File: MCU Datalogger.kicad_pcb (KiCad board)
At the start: 2 copper layers, 52.8 x 34.3 mm, 30 parts, among them J1 Conn_01x04_Pin, J2 Conn_01x09_Pin, J3 Conn_01x04_Pin, J4 Conn_02x03_Odd_Even, U1 24LC1025, U2 DS1337S_, U3 24LC1025, U4 ATMEGA328P-AU, Y1 32.768 KHz, Y2 16 MHz

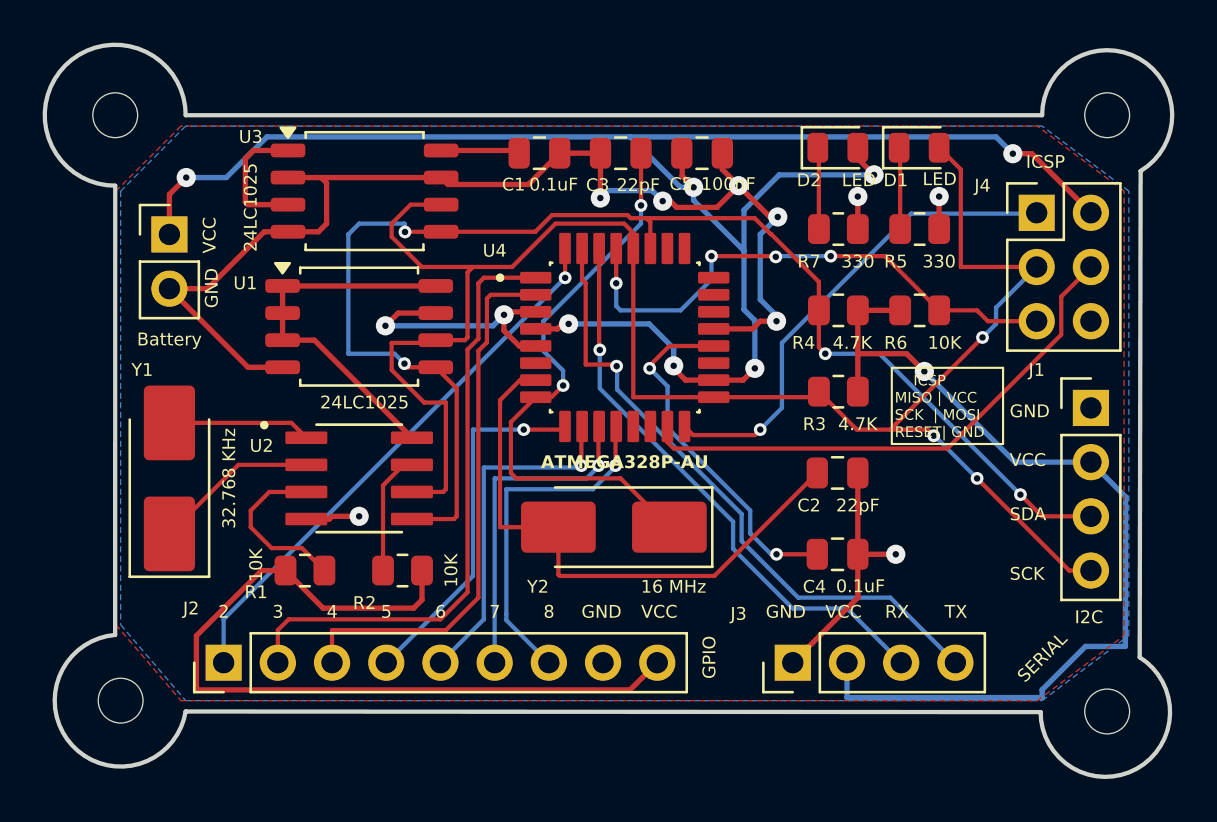
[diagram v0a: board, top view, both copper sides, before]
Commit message: Completed 4-layer PCB routing
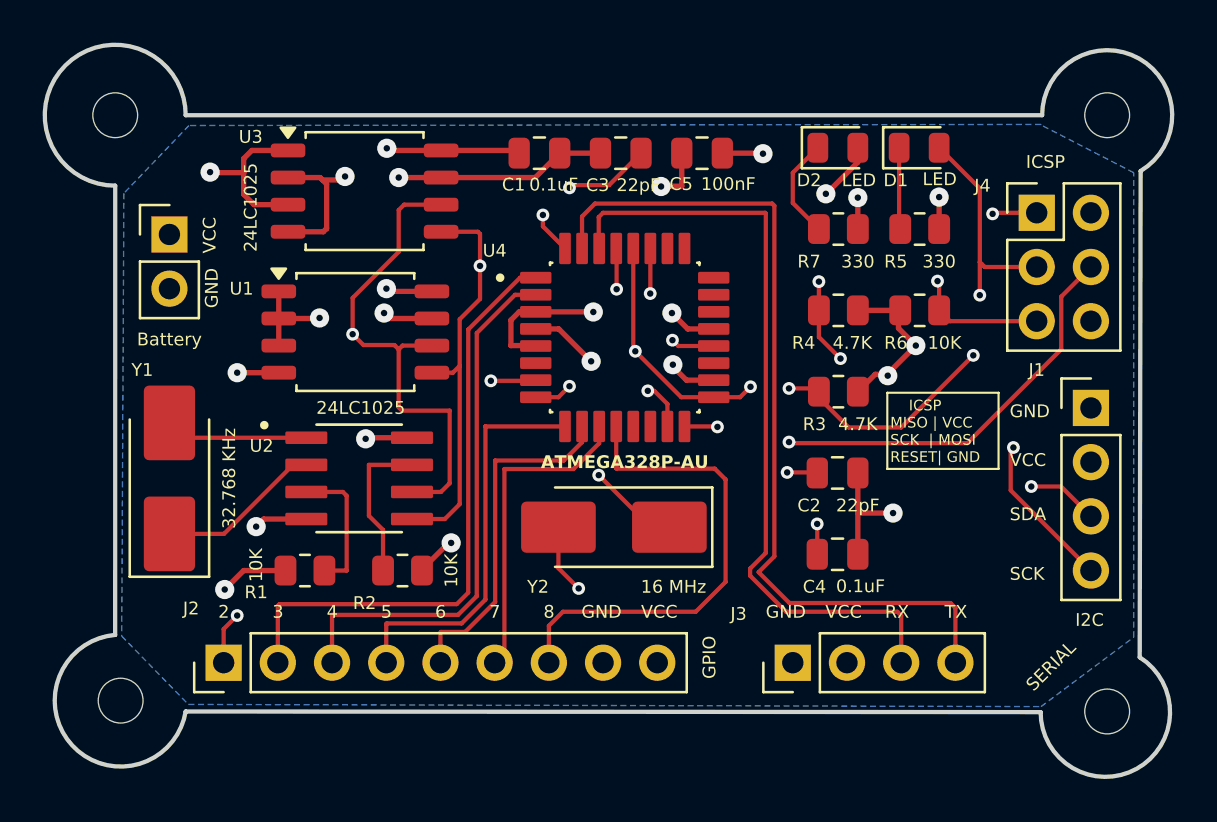
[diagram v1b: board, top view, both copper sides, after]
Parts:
- moved U1 0.31 mm to (45.5, 67.1)
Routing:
- net /VCC: track 196.0 -> 50.8 mm, vias 8 -> 13
- net GND: track 85.9 -> 42.8 mm
- net /TX: track 30.0 -> 40.8 mm, vias 1 -> 0
- net /RX: track 26.8 -> 36.9 mm, vias 1 -> 0
- net /SDA: track 64.3 -> 56.9 mm, vias 4 -> 5
- net /D8: track 16.4 -> 23.0 mm, vias 1 -> 0
- net /MOSI: track 25.3 -> 31.4 mm, vias 0 -> 2
- net Net-(U4-PB6): track 27.1 -> 32.7 mm, vias 0 -> 3
- net /D2: track 26.0 -> 30.3 mm, vias 1 -> 2
- net Net-(U4-PB7): track 27.2 -> 24.2 mm, vias 2 -> 3
- net /SCK: track 86.2 -> 88.3 mm, vias 3 -> 7
- net Net-(U4-AREF): track 16.7 -> 18.7 mm
- net /D5: track 17.0 -> 18.8 mm, vias 1 -> 0
- net /RESET: track 25.5 -> 23.8 mm, vias 4 -> 2
- net Net-(U2-~{INTA}): track 8.04 -> 6.51 mm
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- added copper zone on In2.Cu, net /VCC
- removed copper zone on F.Cu, net /VCC
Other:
- copper layers 2 -> 4
